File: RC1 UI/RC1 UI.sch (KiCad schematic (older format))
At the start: 56 parts, among them J1 KB, J2 RC1_UI_Port, J3 COM, M1 Mounting, M2 Mounting, M3 Mounting, M4 Mounting, Q1 2N3906, Q2 2N3906, Q3 2N3906, Q4 2N3906, Q5 2N3906, Q6 2N3906, U1 74LS145, U2 74LS06, U3 74LS38, U4 74LS00

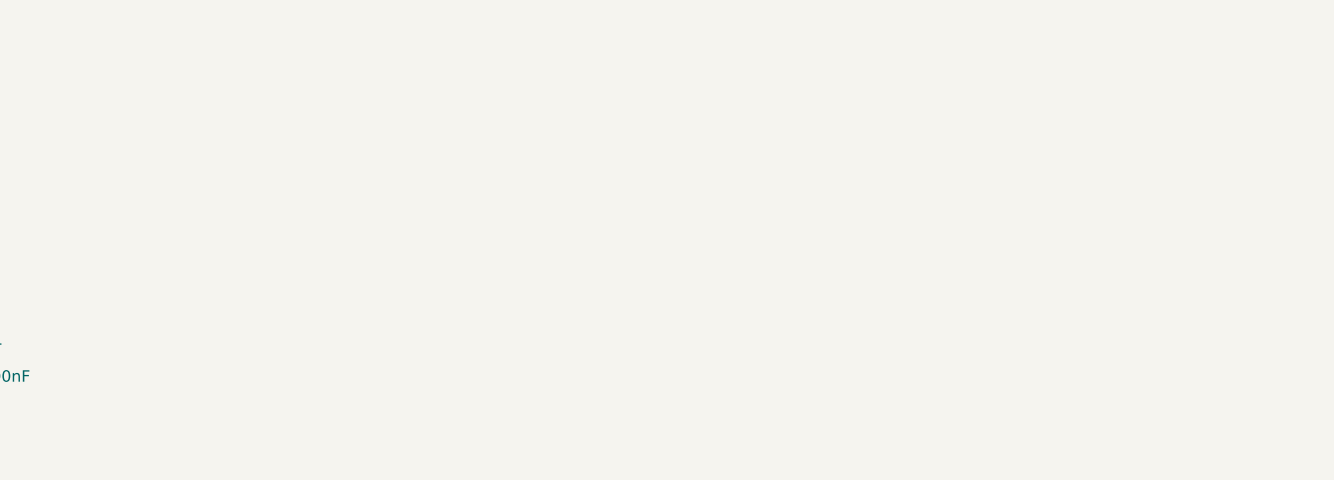
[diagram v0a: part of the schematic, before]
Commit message: Tweaked silkscreens and exported gerbers for CPU/UI
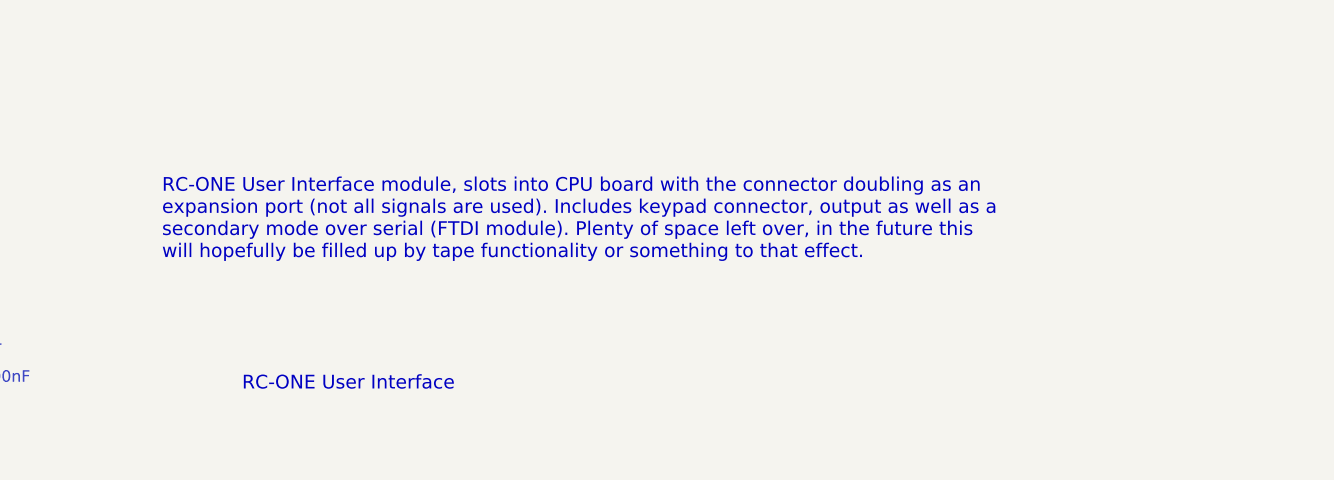
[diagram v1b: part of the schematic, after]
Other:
- note added: "RC-ONE User Interface"
- note added: "RC-ONE User Interface module, slots into CPU board with the connector doubling as an\nexpansion port (not all signals are used). Includes keypad connector, output as well as a\nsecondary mode over serial (FTDI module). Plenty of space left over, in the future this\nwill hopefully be filled up by tape functionality or something to that effect."
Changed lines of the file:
@@
 Wire Wire Line
 	2475 6325 2550 6325
+Text Notes 12175 10925 0    60   ~ 0
+RC-ONE User Interface
+Text Notes 11825 10350 0    60   ~ 0
+RC-ONE User Interface module, slots into CPU board with the connector doubling as an\nexpansion port (not all signals are used). Includes keypad connector, output as well as a\nsecondary mode over serial (FTDI module). Plenty of space left over, in the future this\nwill hopefully be filled up by tape functionality or something to that effect.
 $EndSCHEMATC

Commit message: Reworked schematic to remove 74LS145
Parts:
- removed Q1, Q2, Q3, Q4, Q5, Q6: 2N3906, TO_SOT_Packages_THT:TO-92_Molded_Narrow, symbol 2N3906
- removed R1, R11, R3, R5, R7, R9: 1k, Resistors_THT:R_Axial_DIN0207_L6.3mm_D2.5mm_P5.08mm_Vertical, symbol R
- removed R10, R12, R4, R6, R8: 220, Resistors_THT:R_Axial_DIN0207_L6.3mm_D2.5mm_P5.08mm_Vertical, symbol R
- removed U1: 74LS145, Housings_DIP:DIP-16_W7.62mm_Socket, symbol 74LS145
- removed U2: 74LS06, Housings_DIP:DIP-14_W7.62mm_Socket, symbol 74LS06
- added C?: 100nF, Capacitors_THT:C_Disc_D4.7mm_W2.5mm_P5.00mm, symbol C_Small
- added JP?: DP_EN, symbol Jumper_NC_Dual
- added JP?: SSD_EN, symbol Jumper_NC_Dual
- added JP?: DP4_EN, symbol Jumper_NC_Dual
- added Q2, Q? (x5): 2N3904, TO_SOT_Packages_THT:TO-92_Molded_Narrow, symbol 2N3904
- added R? (x5): 10k, symbol R
- added R? (x2): 100, Resistors_THT:R_Axial_DIN0207_L6.3mm_D2.5mm_P10.16mm_Horizontal, symbol R
- added U? (x2): 74LS138, symbol 74LS138
- added U? (x6): 74LS04, symbol 74LS04
- added U?: 74LS244, symbol 74LS244
- AFF1, AFF2, AFF3, AFF4, AFF5, AFF6: symbol LTS-6960HR -> LTS-6980HR
- J1: value KB -> KEYPAD; symbol Conn_02x08_Counter_Clockwise -> RC1_Keypad_Port
- R14, R15, R16, R17, R18, R19, R20: value 82 -> 100
- R2: value 220 -> 10k; footprint Resistors_THT:R_Axial_DIN0207_L6.3mm_D2.5mm_P5.08mm_Vertical -> (none)
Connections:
- net labels added: DIS1, DIS2, DIS3, DIS4, DIS5, DIS6, DP, DP4, MODE, PB6
- net labels removed: KP_PWR, KP_VCC
- wire segments 269 -> 316
- no-connect marks 15 -> 22
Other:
- note added: "A"
- note added: "B"
- note added: "C"
- note added: "D"
- note added: "KIM-1s 6530 didn't have a\nPB6, but using it for the DP."
- note added: "Q0"
- note added: "Q1"
- note added: "Q2"
- note added: "Q3"
- note added: "Q4"
- note added: "Q5"
- note added: "Q6"
- note added: "Q7"
- note added: "Q8"
- note added: "Q9"
- moved on the sheet: C1, C2, C3, C4, J2, J3, JP1, JP2, JP3, R13, R14, R15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

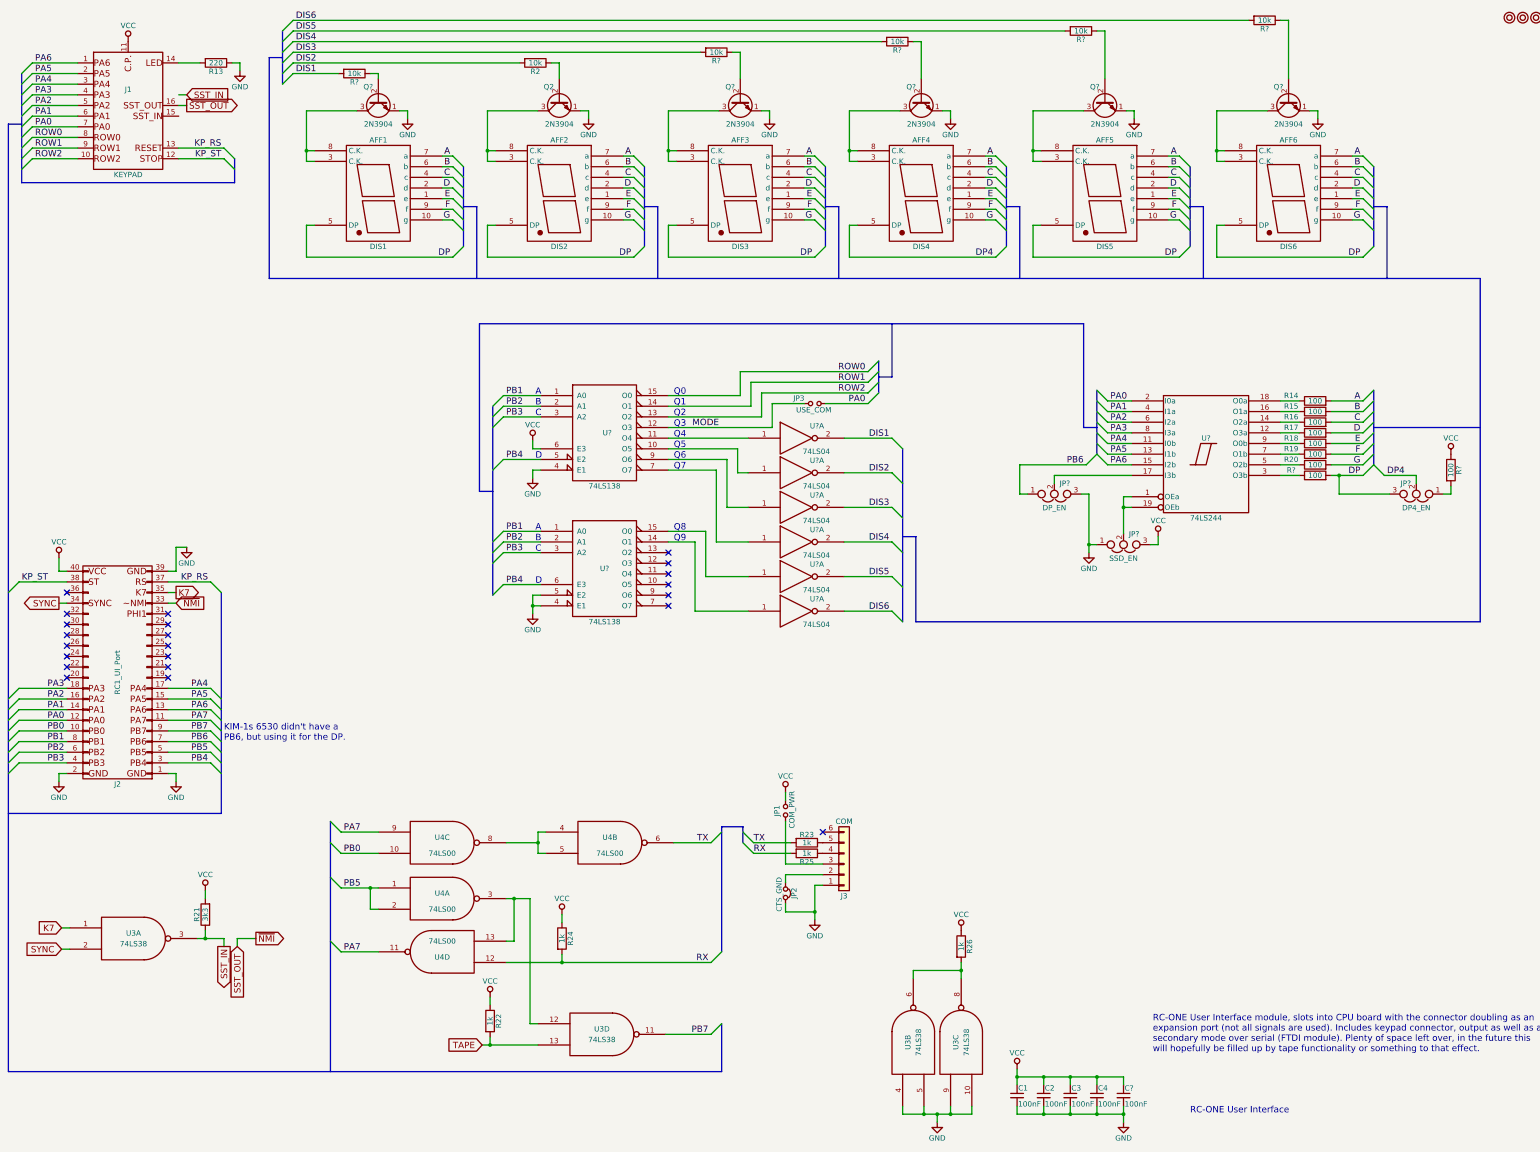
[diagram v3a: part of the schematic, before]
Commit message: Assigned new UI footprints
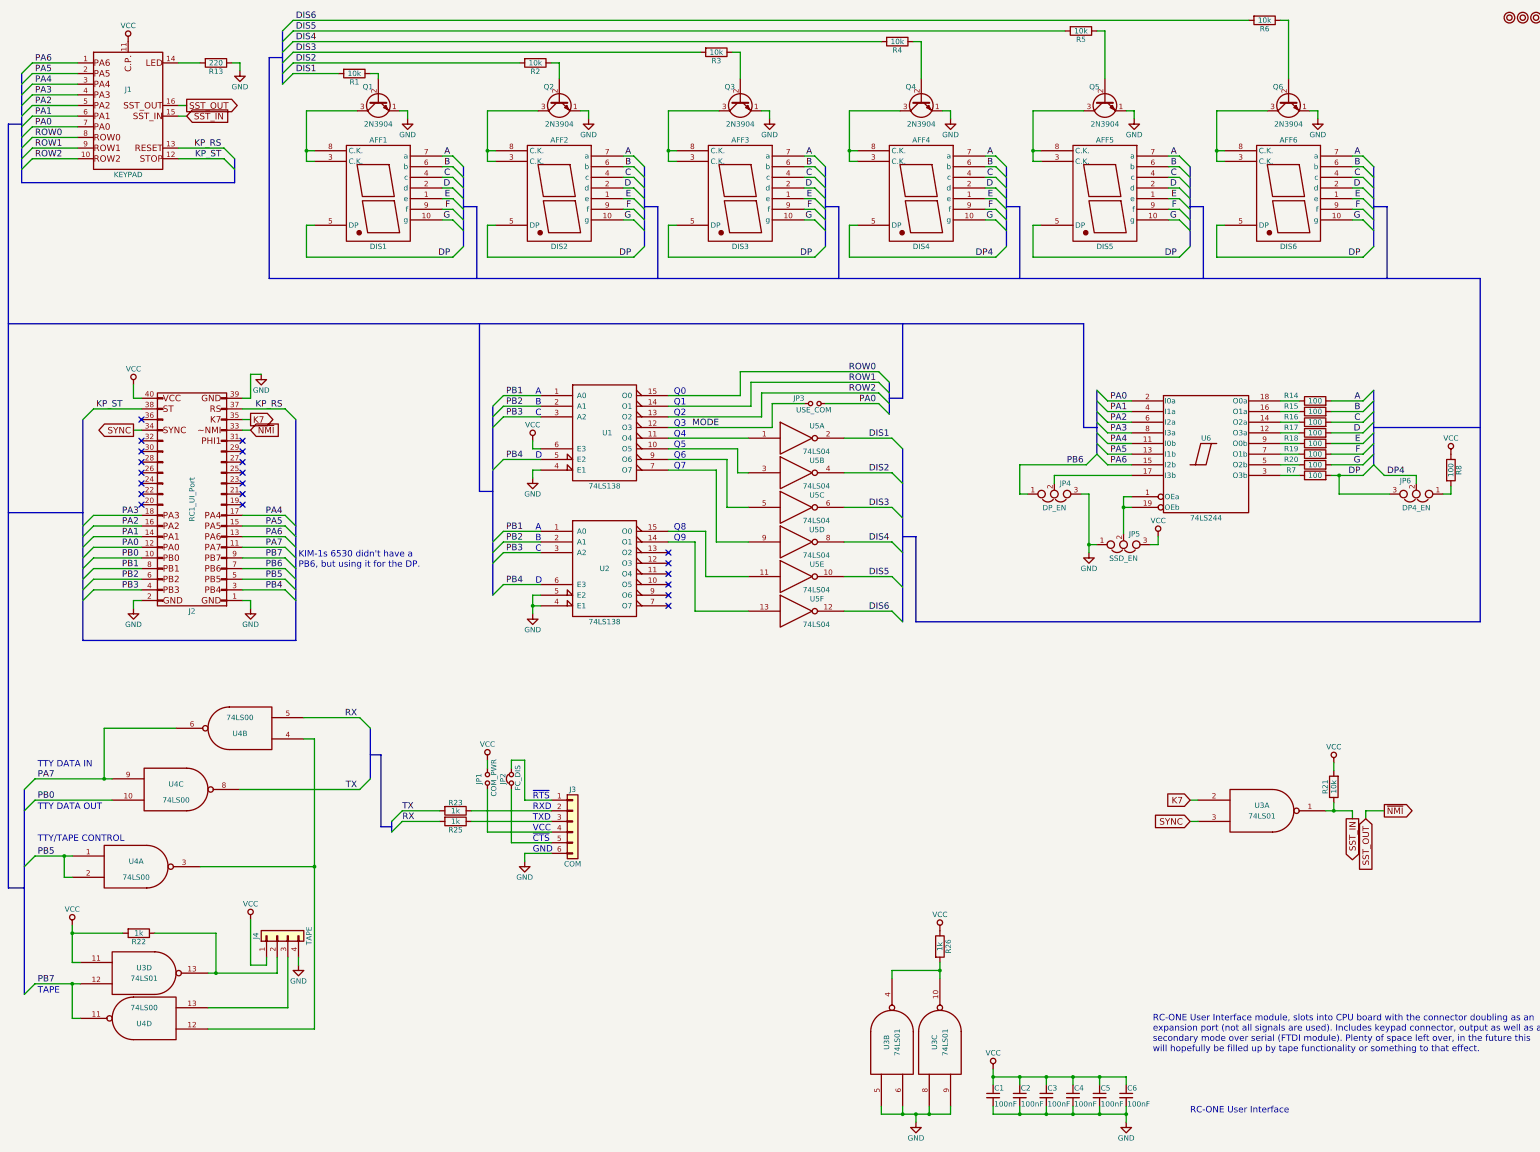
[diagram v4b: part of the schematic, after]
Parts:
- removed R24: 1k, Resistors_THT:R_Axial_DIN0207_L6.3mm_D2.5mm_P10.16mm_Horizontal, symbol R
- removed U3: 74LS38, Housings_DIP:DIP-14_W7.62mm_Socket, symbol 74LS38
- added C6: 100nF, Capacitors_THT:C_Disc_D4.7mm_W2.5mm_P5.00mm, symbol C_Small
- added J4: TAPE, Pin_Headers:Pin_Header_Straight_1x04_Pitch2.54mm, symbol Conn_01x04
- added U3: 74LS01, Housings_DIP:DIP-14_W7.62mm_Socket, symbol 74LS01
- JP2: value CTS_GND -> FC_DIS
- JP4, JP5, JP6: renamed from JP?; footprint (none) -> Pin_Headers:Pin_Header_Straight_1x03_Pitch2.54mm
- R1, R3, R4, R5, R6: renamed from R?; footprint (none) -> Resistors_THT:R_Axial_DIN0207_L6.3mm_D2.5mm_P10.16mm_Horizontal
- R2: footprint (none) -> Resistors_THT:R_Axial_DIN0207_L6.3mm_D2.5mm_P10.16mm_Horizontal
- R21: value 3k3 -> 10k
- U1, U2: renamed from U?; footprint (none) -> Housings_DIP:DIP-16_W7.62mm_Socket
- U5: renamed from U?; footprint (none) -> Housings_DIP:DIP-14_W7.62mm_Socket
- U6: renamed from U?; footprint (none) -> Housings_DIP:DIP-20_W7.62mm_Socket
- gave numbers to parts that had none: 8
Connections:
- net TAPE is gone; now on net VCC: R22.2
- net DIS2: now also U5.4; no longer U5.2
- net DIS3: now also U5.6; no longer U5.2
- net DIS4: now also U5.8; no longer U5.2
- net DIS5: now also U5.10; no longer U5.2
- net DIS6: now also U5.12; no longer U5.2
- net GND: now also J3.6 (Pin_6), C6.2, J4.4 (Pin_4), U3.5, U3.6, U3.7 (GND), U3.7 (GND), U3.7 (GND), U3.7 (GND), U3.8, U3.9; no longer J3.1 (Pin_1), JP2.2
- net K7: now also U3.2
- net PA7: now also U4.6; no longer U4.11
- net PB7: now also U4.11, U3.12
- net RX: now also U4.5; no longer U4.12
- net SST_IN: now also J1.15 (Pin_15), U3.1
- net SYNC: now also U3.3
- net TX: now also U4.8; no longer U4.6
- net VCC: now also C6.1, J4.1 (Pin_1), U3.11, U3.14 (VCC), U3.14 (VCC), U3.14 (VCC), U3.14 (VCC); no longer R22.1
- net at R26.2: now also U3.10, U3.4
- net at U4.3: now also U4.12, U4.4; no longer U4.13
- net at J3.2 (Pin_2): now also R23.1; no longer JP2.1
- net at J3.3 (Pin_3): now also R25.1; no longer JP1.1
- net at J3.4 (Pin_4): now also JP1.1; no longer R25.1
- net at J3.5 (Pin_5): now also JP2.1; no longer R23.1
- net at U2.14 (O1): now also U5.13; no longer U5.1
- net at U2.15 (O0): now also U5.11; no longer U5.1
- net at U1.10 (O5): now also U5.3; no longer U5.1
- net at U1.7 (O7): now also U5.9; no longer U5.1
- net at U1.9 (O6): now also U5.5; no longer U5.1
- new net: J4.2 (Pin_2), R22.1, U3.13
- new net: J4.3 (Pin_3), U4.13
- new net: J3.1 (Pin_1), JP2.2
- no-connect marks 22 -> 21
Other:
- note added: "GND"
- note added: "RXD"
- note added: "TAPE"
- note added: "TTY DATA IN"
- note added: "TTY DATA OUT"
- note added: "TTY/TAPE CONTROL"
- note added: "TXD"
- note added: "VCC"
- note added: "~CTS"
- note added: "~RTS"
- moved on the sheet: C1, C2, C3, C4, C5, J2, J3, JP1, JP2, R21, R22, R23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

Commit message: Layout updated
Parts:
- JP2: value FC_DIS -> FlowControl; footprint Pin_Headers:Pin_Header_Straight_1x02_Pitch2.54mm -> Pin_Headers:Pin_Header_Angled_1x02_Pitch2.54mm
- R1, R2, R3, R4, R5, R6: footprint Resistors_THT:R_Axial_DIN0207_L6.3mm_D2.5mm_P10.16mm_Horizontal -> Resistors_THT:R_Axial_DIN0207_L6.3mm_D2.5mm_P5.08mm_Vertical
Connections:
- net GND: now also R13.2; no longer R13.1
- net RX: now also R25.1; no longer R25.2
- net TX: now also R23.1; no longer R23.2
- net at J1.14 (Pin_14): now also R13.1; no longer R13.2
- net at J3.1 (Pin_1): now also JP2.1; no longer JP2.2
- net at J3.2 (Pin_2): now also R23.2; no longer R23.1
- net at J3.3 (Pin_3): now also R25.2; no longer R25.1
- net at J3.5 (Pin_5): now also JP2.2; no longer JP2.1
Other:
- moved on the sheet: J3, JP2
